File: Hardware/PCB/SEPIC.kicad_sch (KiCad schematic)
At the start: 32 parts, among them Q1 AO3401A, Q2 AO4262E, U1 LM3478MA

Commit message: Backup update
And some fixes of minor issues
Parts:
- removed Q1: AO3401A, Package_TO_SOT_SMD:SOT-23, symbol Transistor_FET:Q_PMOS_GDS
- added Q3: AO4407A, Package_SO:SOIC-8_3.9x4.9mm_P1.27mm, symbol AO4407A:AO4407A
- R7: value 20m -> 10m
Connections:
- net Isen: now also Q2.1 (S_1), Q2.2 (S_2), Q2.3 (S_3); no longer Q2.5 (D_1), Q2.6 (D_2), Q2.7 (D_3), Q2.8 (D_4)
- net Vbus: now also Q3.5 (D_1), Q3.6 (D_2), Q3.7 (D_3), Q3.8 (D_4)
- net Vin: now also Q3.1 (S_1), Q3.2 (S_2), Q3.3 (S_3)
- net at R4.1, Z1.1 (A): now also Q3.4 (G)
- new net: C5.2, L2.2, Q2.5 (D_1), Q2.6 (D_2), Q2.7 (D_3), Q2.8 (D_4)
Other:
- moved on the sheet: C1, C2, D1, D2, Q2, R1, R2, R3, R4, RV1, TP1, TP2

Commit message: Quick fixes
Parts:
- renumbered Q3 to Q1
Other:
- moved on the sheet: C2, C7, C8, C9, L1, Q2, R7, R8, R9, TP3, TP4, U1

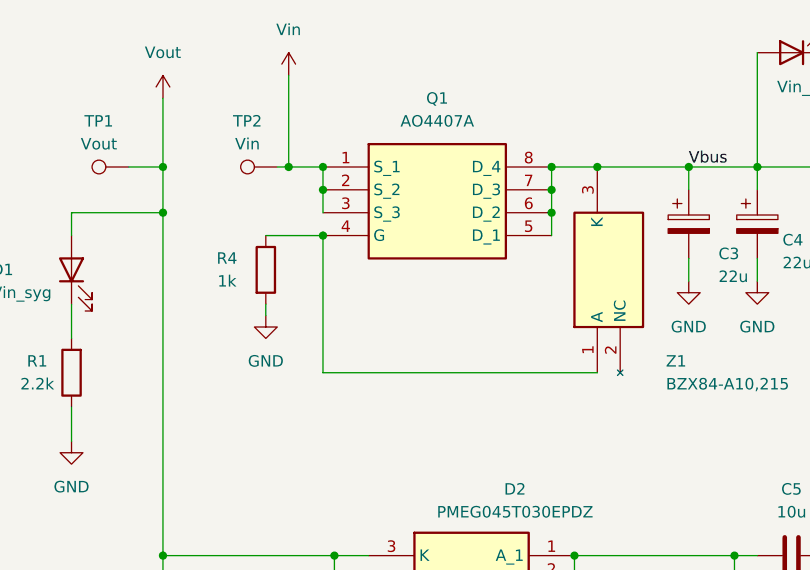
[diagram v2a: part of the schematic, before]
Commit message: Fixed reverser polarity protection circiut mosfet
due the human error the mosfet was connected in reverse
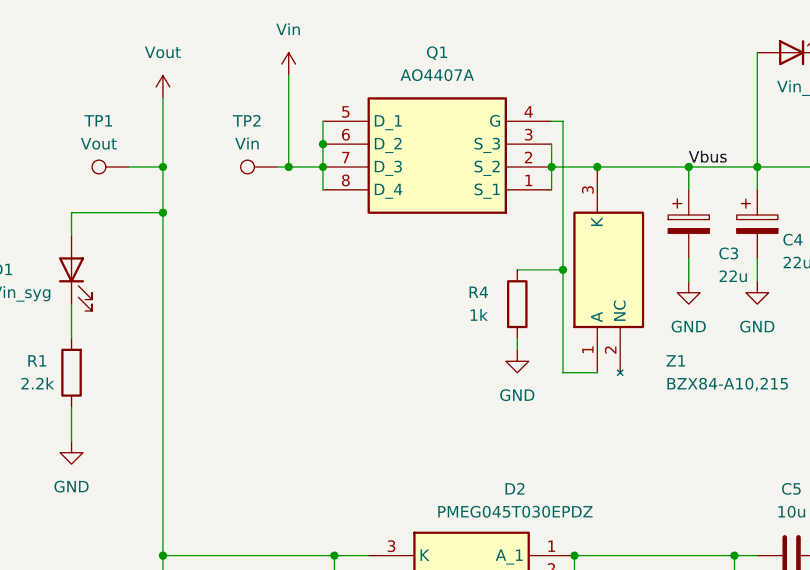
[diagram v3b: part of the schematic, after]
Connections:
- net Vbus: now also Q1.1 (S_1), Q1.2 (S_2), Q1.3 (S_3); no longer Q1.5 (D_1), Q1.6 (D_2), Q1.7 (D_3), Q1.8 (D_4)
- net Vin: now also Q1.5 (D_1), Q1.6 (D_2), Q1.7 (D_3), Q1.8 (D_4); no longer Q1.1 (S_1), Q1.2 (S_2), Q1.3 (S_3)
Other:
- moved on the sheet: Q1, R4
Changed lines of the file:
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@@
 	)
 	(junction
-		(at 74.93 33.02)
+		(at 49.53 27.94)
 		(diameter 0)
 		(color 0 0 0 0)
@@
 	)
 	(junction
-		(at 74.93 30.48)
-		(diameter 0)
-		(color 0 0 0 0)
-	)
-	(junction
 		(at 106.68 30.48)
 		(diameter 0)
@@
 	)
 	(junction
-		(at 49.53 38.1)
-		(diameter 0)
-		(color 0 0 0 0)
-	)
-	(junction
 		(at 80.01 30.48)
 		(diameter 0)
@@
 	)
 	(junction
-		(at 49.53 33.02)
-		(diameter 0)
-		(color 0 0 0 0)
-	)
-	(junction
 		(at 97.79 30.48)
 		(diameter 0)
@@
 	)
 	(junction
-		(at 74.93 35.56)
+		(at 49.53 30.48)
 		(diameter 0)
 		(color 0 0 0 0)
@@
 	)
 	(junction
+		(at 74.93 30.48)
+		(diameter 0)
+		(color 0 0 0 0)
+	)
+	(junction
 		(at 77.47 73.66)
 		(diameter 0)
@@
 	)
 	(junction
-		(at 49.53 30.48)
+		(at 76.2 41.91)
 		(diameter 0)
 		(color 0 0 0 0)
@@
 	(wire
 		(pts
-			(xy 115.57 30.48) (xy 123.19 30.48)
+			(xy 74.93 25.4) (xy 76.2 25.4)
 		)
 		(stroke
@@
 	(wire
 		(pts
-			(xy 49.53 33.02) (xy 49.53 35.56)
+			(xy 115.57 30.48) (xy 123.19 30.48)
 		)
 		(stroke
@@
 	(wire
 		(pts
-			(xy 74.93 33.02) (xy 74.93 35.56)
-		)
-		(stroke
-			(width 0)
-			(type default)
-		)
-	)
-	(wire
-		(pts
 			(xy 123.19 39.37) (xy 123.19 38.1)
 		)
@@
 	(wire
 		(pts
+			(xy 74.93 27.94) (xy 74.93 30.48)
+		)
+		(stroke
+			(width 0)
+			(type default)
+		)
+	)
+	(wire
+		(pts
 			(xy 31.75 115.57) (xy 31.75 118.11)
 		)
@@
 	(wire
 		(pts
+			(xy 49.53 30.48) (xy 49.53 33.02)
+		)
+		(stroke
+			(width 0)
+			(type default)
+		)
+	)
+	(wire
+		(pts
 			(xy 31.75 100.33) (xy 31.75 105.41)
 		)
@@
 	(wire
 		(pts
+			(xy 76.2 25.4) (xy 76.2 41.91)
+		)
+		(stroke
+			(width 0)
+			(type default)
+		)
+	)
+	(wire
+		(pts
 			(xy 27.94 30.48) (xy 31.75 30.48)
 		)
@@
 	(wire
 		(pts
+			(xy 49.53 27.94) (xy 49.53 30.48)
+		)
+		(stroke
+			(width 0)
+			(type default)
+		)
+	)
+	(wire
+		(pts
 			(xy 97.79 43.18) (xy 97.79 40.64)
 		)
@@
 	(wire
 		(pts
-			(xy 43.18 38.1) (xy 49.53 38.1)
+			(xy 71.12 41.91) (xy 76.2 41.91)
 		)
 		(stroke
@@
 	(wire
 		(pts
-			(xy 49.53 53.34) (xy 49.53 38.1)
+			(xy 76.2 53.34) (xy 76.2 41.91)
 		)
 		(stroke
@@
 	(wire
 		(pts
+			(xy 49.53 25.4) (xy 49.53 27.94)
+		)
+		(stroke
+			(width 0)
+			(type default)
+		)
+	)
+	(wire
+		(pts
 			(xy 77.47 73.66) (xy 77.47 76.2)
 		)
@@
 	(wire
 		(pts
-			(xy 43.18 45.72) (xy 43.18 46.99)
+			(xy 71.12 49.53) (xy 71.12 50.8)
 		)
 		(stroke
@@
 	(wire
 		(pts
-			(xy 49.53 30.48) (xy 49.53 33.02)
-		)
-		(stroke
-			(width 0)
-			(type default)
-		)
-	)
-	(wire
-		(pts
 			(xy 123.19 30.48) (xy 154.94 30.48)
 		)
@@
 	(wire
 		(pts
-			(xy 49.53 53.34) (xy 80.01 53.34)
+			(xy 76.2 53.34) (xy 80.01 53.34)
 		)
 		(stroke
@@
 		)
 	)
-	(wire
-		(pts
-			(xy 74.93 35.56) (xy 74.93 38.1)
-		)
-		(stroke
-			(width 0)
-			(type default)
-		)
-	)
 	(image
 		(at 185.42 111.76)
@@
 	(symbol
 		(lib_id "power:GND")
-		(at 43.18 46.99 0)
+		(at 71.12 50.8 0)
 		(unit 1)
 		(body_style 1)
@@
 		(fields_autoplaced yes)
 		(property "Reference" "#PWR06"
-			(at 43.18 53.34 0)
+			(at 71.12 57.15 0)
 			(hide yes)
 			(show_name no)
@@
 		)
 		(property "Value" "GND"
-			(at 43.18 52.07 0)
+			(at 71.12 55.88 0)
 			(show_name no)
 			(do_not_autoplace no)
@@
 		)
 		(property "Footprint" ""
-			(at 43.18 46.99 0)
+			(at 71.12 50.8 0)
 			(hide yes)
 			(show_name no)
@@
 		)
 		(property "Datasheet" ""
-			(at 43.18 46.99 0)
+			(at 71.12 50.8 0)
 			(hide yes)
 			(show_name no)
@@
 		)
 		(property "Description" "Power symbol creates a global label with name \"GND\" , ground"
-			(at 43.18 46.99 0)
+			(at 71.12 50.8 0)
 			(hide yes)
 			(show_name no)
@@
 	(symbol
 		(lib_id "AO4407A:AO4407A")
-		(at 49.53 30.48 0)
+		(at 74.93 33.02 180)
 		(unit 1)
 		(body_style 1)
@@
 		(fields_autoplaced yes)
 		(property "Reference" "Q1"
-			(at 62.23 22.86 0)
+			(at 62.23 17.78 0)
 			(show_name no)
 			(do_not_autoplace no)
@@
 		)
 		(property "Value" "AO4407A"
-			(at 62.23 25.4 0)
+			(at 62.23 20.32 0)
 			(show_name no)
 			(do_not_autoplace no)
@@
 		)
 		(property "Footprint" "Package_SO:SOIC-8_3.9x4.9mm_P1.27mm"
-			(at 71.12 125.4 0)
+			(at 53.34 -61.9 0)
 			(hide yes)
 			(show_name no)
@@
 		)
 		(property "Datasheet" "http://aosmd.com/res/data_sheets/AO4407A.pdf"
-			(at 71.12 225.4 0)
+			(at 53.34 -161.9 0)
 			(hide yes)
 			(show_name no)
@@
 		)
 		(property "Description" "30V P-Channel MOSFET"
-			(at 49.53 30.48 0)
+			(at 74.93 33.02 0)
 			(hide yes)
 			(show_name no)
@@
 		)
 		(property "Height" "1.75"
-			(at 71.12 425.4 0)
+			(at 53.34 -361.9 0)
 			(hide yes)
 			(show_name no)
@@
 		)
 		(property "TME Electronic Components Part Number" ""
-			(at 71.12 525.4 0)
+			(at 53.34 -461.9 0)
 			(hide yes)
 			(show_name no)
@@
 		)
 		(property "TME Electronic Components Price/Stock" ""
-			(at 71.12 625.4 0)
+			(at 53.34 -561.9 0)
 			(hide yes)
 			(show_name no)
@@
 		)
 		(property "Manufacturer_Name" "Alpha & Omega Semiconductors"
-			(at 71.12 725.4 0)
+			(at 53.34 -661.9 0)
 			(hide yes)
 			(show_name no)
@@
 		)
 		(property "Manufacturer_Part_Number" "AO4407A"
-			(at 71.12 825.4 0)
+			(at 53.34 -761.9 0)
 			(hide yes)
 			(show_name no)
@@
 	(symbol
 		(lib_id "Device:R")
-		(at 43.18 41.91 0)
+		(at 71.12 45.72 0)
 		(unit 1)
 		(body_style 1)
@@
 		(dnp no)
 		(property "Reference" "R4"
-			(at 38.862 40.64 0)
+			(at 66.802 44.45 0)
 			(show_name no)
 			(do_not_autoplace no)
@@
 		)
 		(property "Value" "1k"
-			(at 38.862 43.18 0)
+			(at 66.802 46.99 0)
 			(show_name no)
 			(do_not_autoplace no)
@@
 		)
 		(property "Footprint" "Resistor_SMD:R_1206_3216Metric"
-			(at 41.402 41.91 90)
+			(at 69.342 45.72 90)
 			(hide yes)
 			(show_name no)
@@
 		)
 		(property "Datasheet" ""
-			(at 43.18 41.91 0)
+			(at 71.12 45.72 0)
 			(hide yes)
 			(show_name no)
@@
 		)
 		(property "Description" "Resistor"
-			(at 43.18 41.91 0)
+			(at 71.12 45.72 0)
 			(hide yes)
 			(show_name no)

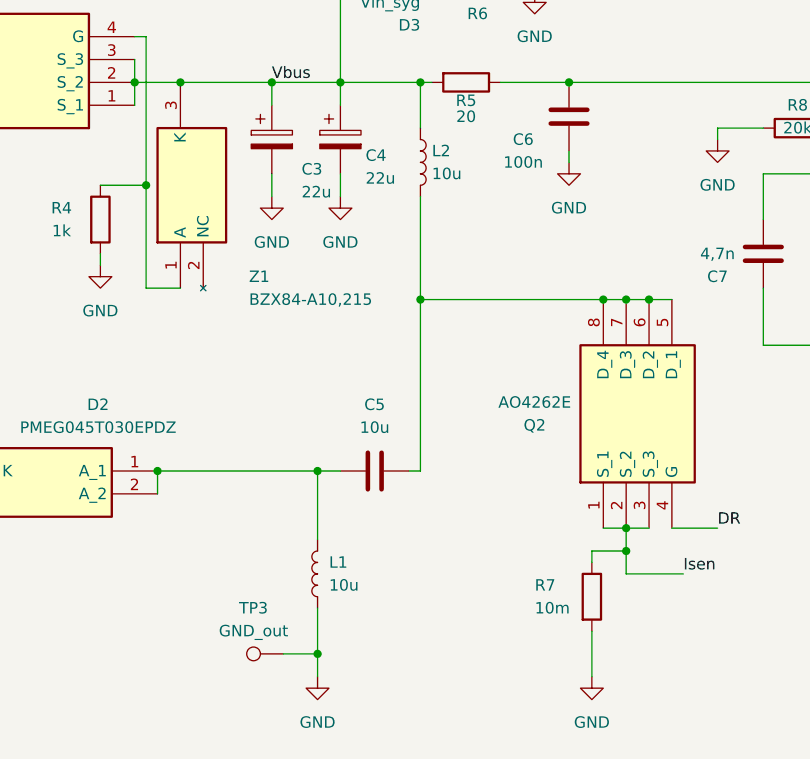
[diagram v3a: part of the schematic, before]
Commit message: Placed actual coils footprints
Used this:
https://www.tme.eu/pl/details/hcm0703-4r7-r/dlawiki/eaton-electronics/
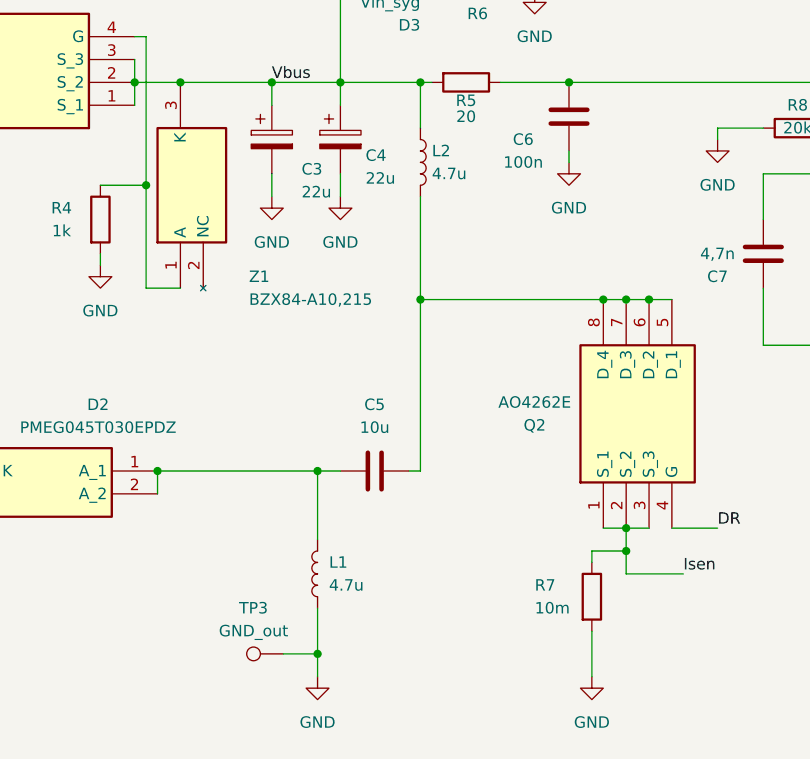
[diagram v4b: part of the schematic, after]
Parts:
- L1, L2: value 10u -> 4.7u; footprint Inductor_SMD:L_Vishay_IHLP-2020 -> HCM0703-4R7-R:INDPM7166X300N
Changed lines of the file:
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@@
 			)
 		)
-		(property "Value" "10u"
+		(property "Value" "4.7u"
 			(at 107.95 40.6399 0)
 			(show_name no)
@@
 			)
 		)
-		(property "Footprint" "Inductor_SMD:L_Vishay_IHLP-2020"
+		(property "Footprint" "HCM0703-4R7-R:INDPM7166X300N"
 			(at 106.68 39.37 0)
 			(hide yes)
@@
 			)
 		)
-		(property "Value" "10u"
+		(property "Value" "4.7u"
 			(at 96.52 86.3599 0)
 			(show_name no)
@@
 			)
 		)
-		(property "Footprint" "Inductor_SMD:L_Vishay_IHLP-2020"
+		(property "Footprint" "HCM0703-4R7-R:INDPM7166X300N"
 			(at 95.25 85.09 0)
 			(hide yes)
